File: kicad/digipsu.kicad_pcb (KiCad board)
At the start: 2 copper layers, 137.2 x 174 mm, 154 parts, among them J1 Screw_Terminal_01x03, J2 PWR IN, J3 8P8C, J4 8P8C, J5 8P8C, Q1 BC327, Q2 BC337, Q3 2N6058, Q4 2N6058, Q5 IRLZ34N, SW1 RotaryEncoder_Switch, SW2 RotaryEncoder_Switch, U1 INA169, U10 Pico, U11 M24C32-RMN, U12 SN75176BP, U13 6N137, U14 SN75176BP, U15 SN75176BP, U16 74AC14, U2 MCP6002-xP, U3 Pico, U301 74AC14, U4 MCP6002-xP, U5 L7805, U6 MCP3464R, U7 LF33_TO220, U8 6N137, U9 SN75176BP

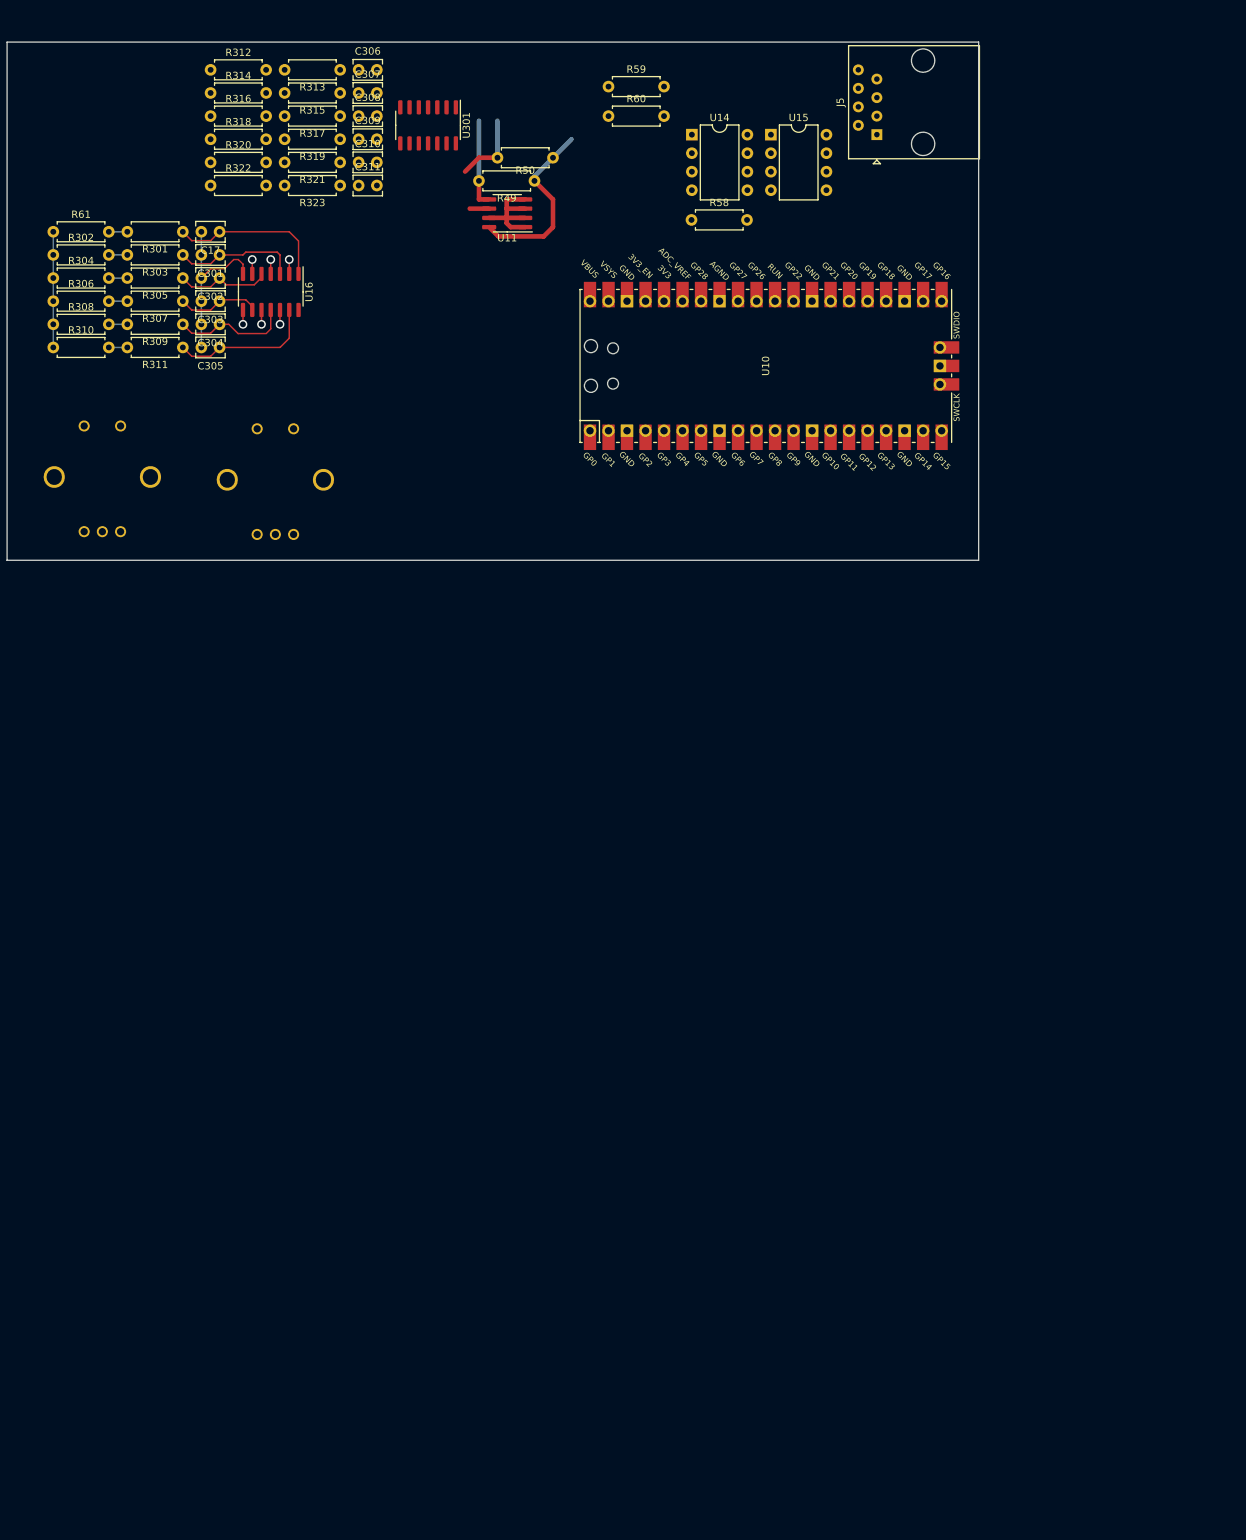
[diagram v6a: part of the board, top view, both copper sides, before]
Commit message: Start UI pcb design
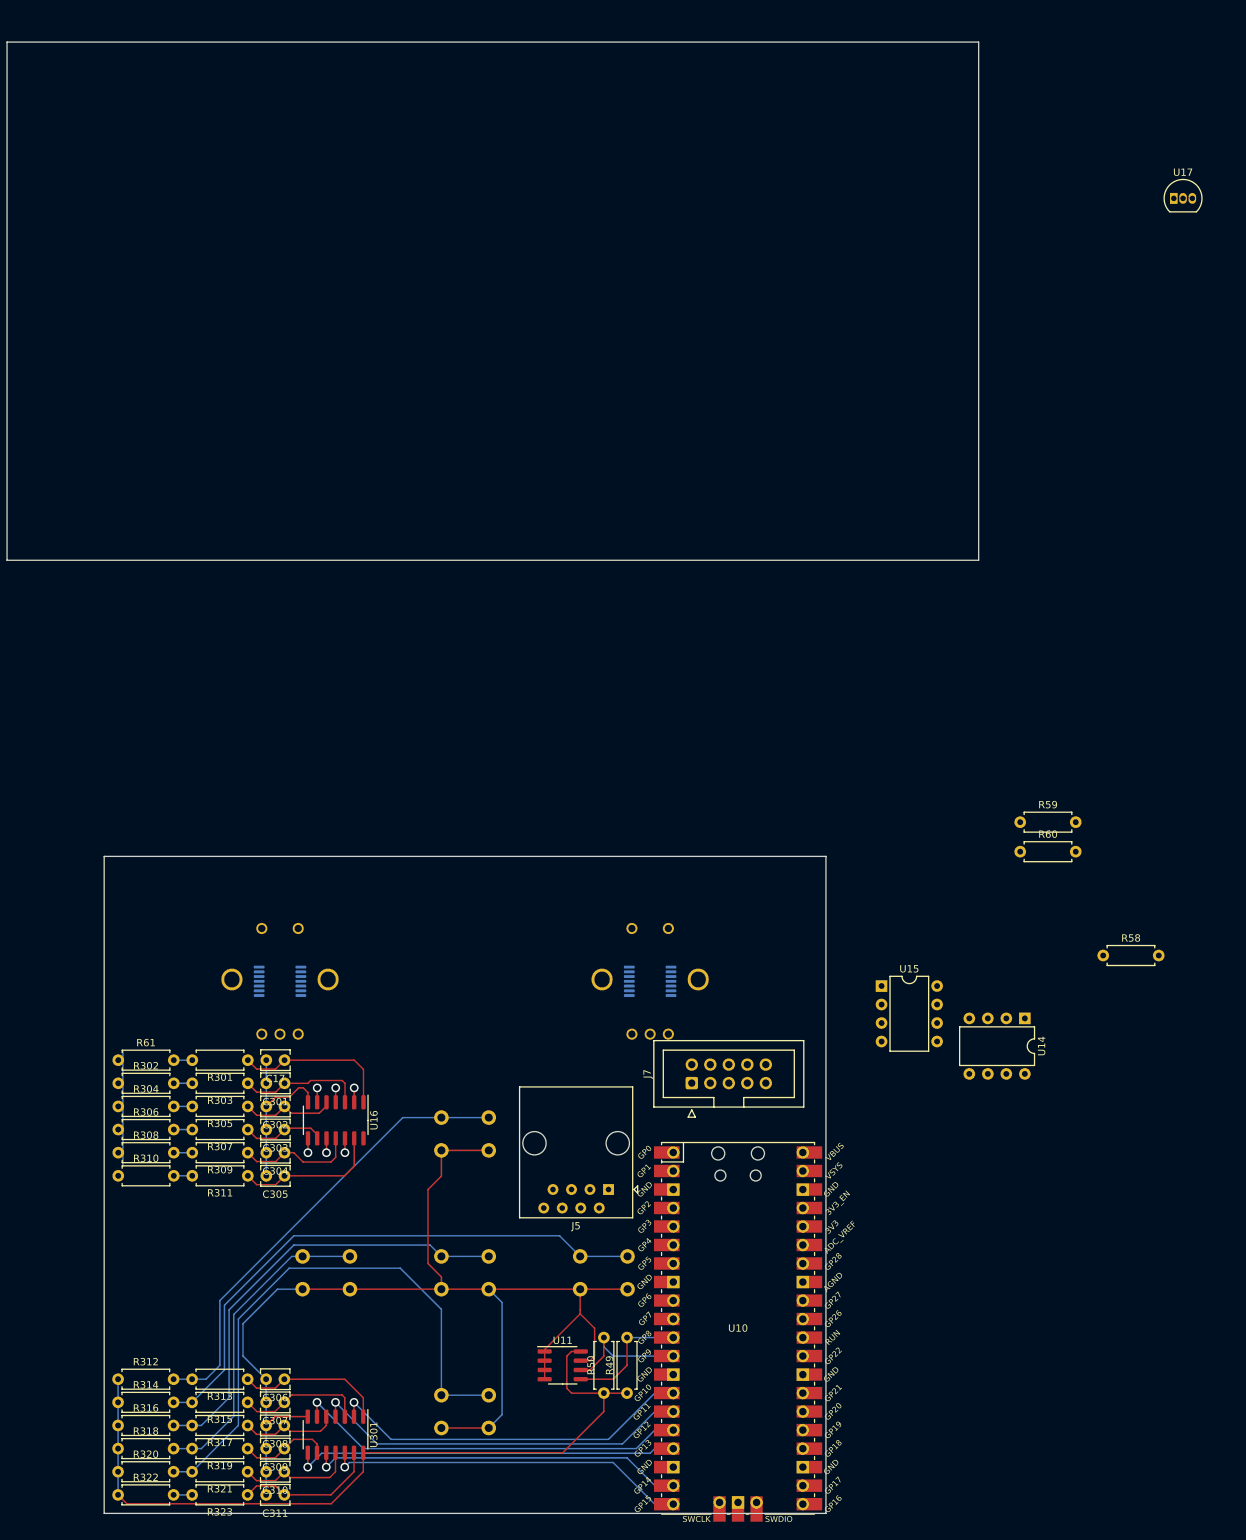
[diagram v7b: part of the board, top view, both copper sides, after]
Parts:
- added J7: Conn_02x05_Odd_Even, Connector_IDC:IDC-Header_2x05_P2.54mm_Vertical, F.Cu at (111.8, 267.3)
- added SW301: SW_Push_45deg, Button_Switch_THT:SW_PUSH_6mm, B.Cu at (102.9, 291.1)
- added SW302: SW_Push_45deg, Button_Switch_THT:SW_PUSH_6mm, B.Cu at (83.9, 272.1)
- added SW303: SW_Push_45deg, Button_Switch_THT:SW_PUSH_6mm, B.Cu at (83.9, 291.1)
- added SW304: SW_Push_45deg, Button_Switch_THT:SW_PUSH_6mm, B.Cu at (64.8, 291.1)
- added SW305: SW_Push_45deg, Button_Switch_THT:SW_PUSH_6mm, B.Cu at (83.9, 310.2)
- added U17: DS1822, Package_TO_SOT_THT:TO-92_Inline, F.Cu at (177.9, 145.9)
- added U18: AS5047D, Package_SO:TSSOP-14_4.4x5mm_P0.65mm, B.Cu at (55.2, 253.4)
- added U19: AS5047D, Package_SO:TSSOP-14_4.4x5mm_P0.65mm, B.Cu at (106.0, 253.4)
- moved U301 180.2 mm to (62.9, 315.6)
- moved R312 180.2 mm to (33.0, 308.0)
- moved R313 180.2 mm to (50.8, 308.0)
- moved R318 180.2 mm to (33.0, 317.5)
- moved R319 180.2 mm to (50.8, 317.5)
- moved R320 180.2 mm to (33.0, 320.7)
- moved R321 180.2 mm to (50.8, 320.7)
- moved R322 180.2 mm to (33.0, 323.9)
- moved R323 180.2 mm to (50.8, 323.9)
- moved R314 180.2 mm to (33.0, 311.1)
- moved R315 180.2 mm to (50.8, 311.1)
- moved R316 180.2 mm to (33.0, 314.3)
- moved R317 180.2 mm to (50.8, 314.3)
- moved C306 180.0 mm to (55.8, 308.0), turned to 180 degrees
- moved C309 180.0 mm to (55.8, 317.5), turned to 180 degrees
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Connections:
- net +3.3V renamed /User Interface/+3.3V
- net Net-(R312-Pad2) renamed /User Interface/SWin7
- net Net-(R314-Pad2) renamed /User Interface/SWin8
- net Net-(R316-Pad2) renamed /User Interface/SWin9
- net Net-(R318-Pad2) renamed /User Interface/SWin10
- net Net-(R320-Pad2) renamed /User Interface/SWin11
- net Net-(R322-Pad2) renamed /User Interface/SWin12
- R49 pad 2: Net-(U11-SDA) -> /User Interface/SDA
- R50 pad 2: Net-(U11-SCL) -> /User Interface/SCL
- U10 pad 11: unconnected-(U10-GPIO8-Pad11) -> /User Interface/SDA
- U10 pad 12: unconnected-(U10-GPIO9-Pad12) -> /User Interface/SCL
- U10 pad 14: unconnected-(U10-GPIO10-Pad14) -> /User Interface/SWout7
- U10 pad 15: unconnected-(U10-GPIO11-Pad15) -> /User Interface/SWout8
- U10 pad 16: unconnected-(U10-GPIO12-Pad16) -> /User Interface/SWout9
- U10 pad 17: unconnected-(U10-GPIO13-Pad17) -> /User Interface/SWout10
- U10 pad 19: unconnected-(U10-GPIO14-Pad19) -> /User Interface/SWout11
- U10 pad 20: unconnected-(U10-GPIO15-Pad20) -> /User Interface/SWout12
- U11 pad 1: GNDD -> /User Interface/GND
- U11 pad 2: GNDD -> /User Interface/GND
- U11 pad 3: GNDD -> /User Interface/GND
- U11 pad 4: GNDD -> /User Interface/GND
- U11 pad 5: Net-(U11-SDA) -> /User Interface/SDA
- U11 pad 6: Net-(U11-SCL) -> /User Interface/SCL
- U11 pad 7: GNDD -> /User Interface/GND
- U301 pad 10: unconnected-(U301-Pad10) -> /User Interface/SWout11
- U301 pad 12: unconnected-(U301-Pad12) -> /User Interface/SWout12
- U301 pad 2: unconnected-(U301-Pad2) -> /User Interface/SWout7
- U301 pad 4: unconnected-(U301-Pad4) -> /User Interface/SWout8
- U301 pad 6: unconnected-(U301-Pad6) -> /User Interface/SWout9
- U301 pad 8: unconnected-(U301-Pad8) -> /User Interface/SWout10
- U4 pad 2: GND -> /VoltageSense
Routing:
- net /User Interface/GND: track 24.2 -> 187.3 mm
- net /User Interface/+3.3V: track 40.9 -> 123.4 mm
- net /User Interface/SWin8: track 0.00 -> 78.2 mm
- net /User Interface/SWin11: track 0.00 -> 77.5 mm
- net /User Interface/SWin7: track 0.00 -> 63.3 mm
- net /User Interface/SWin9: track 0.00 -> 61.2 mm
- net /User Interface/SWout9: track 0.00 -> 54.5 mm, vias 0 -> 1
- net /User Interface/SWout10: track 0.00 -> 53.2 mm, vias 0 -> 1
- net /User Interface/SWout8: track 0.00 -> 52.5 mm, vias 0 -> 1
- net /User Interface/SWout11: track 0.00 -> 51.7 mm, vias 0 -> 1
- net /User Interface/SWout7: track 0.00 -> 50.5 mm, vias 0 -> 1
- net /User Interface/SWout12: track 0.00 -> 49.7 mm, vias 0 -> 1
- net /User Interface/SWin10: track 0.00 -> 43.3 mm
- net Net-(C306-Pad1): track 0.00 -> 20.5 mm
- net Net-(C311-Pad1): track 0.00 -> 19.5 mm
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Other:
- board size 137.2 x 174 mm -> 137.2 x 304.8 mm

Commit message: Continue on UI board design
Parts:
- added C18: 100n, Capacitor_THT:C_Disc_D3.8mm_W2.6mm_P2.50mm, F.Cu at (39.4, 246.0)
- added C19: 100n, Capacitor_THT:C_Disc_D3.8mm_W2.6mm_P2.50mm, F.Cu at (39.4, 250.2)
- moved R59 82.6 mm to (165.1, 313.7), turned to 90 degrees
- moved R60 78.2 mm to (161.3, 313.7), turned to 90 degrees
- moved R58 60.5 mm to (146.1, 306.1), turned to -90 degrees
- moved U15 55.7 mm to (157.5, 306.1), turned to -90 degrees
- moved U14 55.1 mm to (182.9, 307.3)
- moved R50 50.4 mm to (148.5, 297.2)
- moved U11 50.4 mm to (142.8, 293.4)
- moved R49 50.4 mm to (151.6, 297.2)
- moved J5 30.5 mm to (99.1, 312.4)
- moved J7 20.3 mm to (91.4, 267.5)
- moved C306 10.8 mm to (55.8, 297.2)
- moved C308 10.8 mm to (55.8, 303.5)
- moved C309 10.8 mm to (55.8, 306.7)
- moved C310 10.8 mm to (55.8, 309.9)
- moved C311 10.8 mm to (55.8, 313.1)
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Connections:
- net /User Interface/CTRL.+5V renamed /User Interface/+5V
- J5 pad 1: /User Interface/CTRL.GND -> /User Interface/GND
- R59 pad 1: unconnected-(R59-Pad1) -> /User Interface/GND
- U10 pad 1: /User Interface/SWout1 -> /User Interface/TX
- U10 pad 10: unconnected-(U10-GPIO7-Pad10) -> /User Interface/SWout6
- U10 pad 14: /User Interface/SWout7 -> unconnected-(U10-GPIO10-Pad14)
- U10 pad 15: /User Interface/SWout8 -> unconnected-(U10-GPIO11-Pad15)
- U10 pad 16: /User Interface/SWout9 -> unconnected-(U10-GPIO12-Pad16)
- U10 pad 17: /User Interface/SWout10 -> unconnected-(U10-GPIO13-Pad17)
- U10 pad 19: /User Interface/SWout11 -> unconnected-(U10-GPIO14-Pad19)
- U10 pad 2: /User Interface/SWout2 -> /User Interface/RX
- U10 pad 20: /User Interface/SWout12 -> unconnected-(U10-GPIO15-Pad20)
- U10 pad 21: unconnected-(U10-GPIO16-Pad21) -> /User Interface/SWout12
- U10 pad 22: unconnected-(U10-GPIO17-Pad22) -> /User Interface/SWout11
- U10 pad 24: unconnected-(U10-GPIO18-Pad24) -> /User Interface/SWout10
- U10 pad 25: unconnected-(U10-GPIO19-Pad25) -> /User Interface/SWout9
- U10 pad 26: unconnected-(U10-GPIO20-Pad26) -> /User Interface/SWout8
- U10 pad 27: unconnected-(U10-GPIO21-Pad27) -> /User Interface/SWout7
- U10 pad 36: unconnected-(U10-3V3-Pad36) -> /User Interface/+3.3V
- U10 pad 38: /User Interface/CTRL.GND -> /User Interface/GND
- U10 pad 4: /User Interface/SWout3 -> /User Interface/SWout1
- U10 pad 5: /User Interface/SWout4 -> /User Interface/SWout2
- U10 pad 6: /User Interface/SWout5 -> /User Interface/SWout3
- U10 pad 7: /User Interface/SWout6 -> /User Interface/SWout4
- U10 pad 9: unconnected-(U10-GPIO6-Pad9) -> /User Interface/SWout5
- U14 pad 5: /User Interface/CTRL.GND -> /User Interface/GND
- U15 pad 2: /User Interface/CTRL.GND -> /User Interface/GND
- U15 pad 3: /User Interface/CTRL.GND -> /User Interface/GND
- U15 pad 5: /User Interface/CTRL.GND -> /User Interface/GND
- U18 pad 1: unconnected-(U18-~{CS}-Pad1) -> /User Interface/ENC.CS1
- U18 pad 11: unconnected-(U18-VDD-Pad11) -> Net-(U18-VDD)
- U18 pad 12: unconnected-(U18-VDD3V3-Pad12) -> Net-(U18-VDD)
- U18 pad 13: unconnected-(U18-GND-Pad13) -> /User Interface/GND
- U18 pad 2: unconnected-(U18-CLK-Pad2) -> /User Interface/ENC.CLK
- U18 pad 3: unconnected-(U18-MISO-Pad3) -> /User Interface/ENC.MISO
- U18 pad 4: unconnected-(U18-MOSI-Pad4) -> /User Interface/ENC.MOSI
- U18 pad 5: unconnected-(U18-TST-Pad5) -> /User Interface/GND
- U18 pad 6: unconnected-(U18-B-Pad6) -> /User Interface/SWout2
- U18 pad 7: unconnected-(U18-A-Pad7) -> /User Interface/SWout2
- U19 pad 1: unconnected-(U19-~{CS}-Pad1) -> /User Interface/ENC.CS2
- U19 pad 11: unconnected-(U19-VDD-Pad11) -> Net-(U19-VDD)
- U19 pad 12: unconnected-(U19-VDD3V3-Pad12) -> Net-(U19-VDD)
- U19 pad 13: unconnected-(U19-GND-Pad13) -> /User Interface/GND
- U19 pad 2: unconnected-(U19-CLK-Pad2) -> /User Interface/ENC.CLK
- U19 pad 3: unconnected-(U19-MISO-Pad3) -> /User Interface/ENC.MISO
- U19 pad 4: unconnected-(U19-MOSI-Pad4) -> /User Interface/ENC.MOSI
- U19 pad 5: unconnected-(U19-TST-Pad5) -> /User Interface/GND
- U19 pad 6: unconnected-(U19-B-Pad6) -> /User Interface/SWout6
- U19 pad 7: unconnected-(U19-A-Pad7) -> /User Interface/SWout5
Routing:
- net /User Interface/SWin8: track 78.2 -> 9.04 mm
- net /User Interface/SWin11: track 77.5 -> 9.04 mm
- net /User Interface/SWin7: track 63.3 -> 9.04 mm
- net /User Interface/SWout9: track 54.5 -> 1.97 mm
- net /User Interface/SWin9: track 61.2 -> 9.04 mm
- net /User Interface/SWout10: track 53.2 -> 1.97 mm
- net /User Interface/SWout8: track 52.5 -> 1.97 mm
- net /User Interface/SWout11: track 51.7 -> 1.97 mm
- net /User Interface/SWout7: track 50.5 -> 1.97 mm
- net /User Interface/SWout12: track 49.7 -> 1.97 mm
- net /User Interface/+3.3V: track 123.4 -> 85.5 mm
- net /User Interface/SWin10: track 43.3 -> 9.04 mm
- net /User Interface/GND: track 187.3 -> 156.3 mm
- net /User Interface/CTRL.RX-: track 0.00 -> 12.8 mm
- net /User Interface/CTRL.RX+: track 0.00 -> 12.8 mm
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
